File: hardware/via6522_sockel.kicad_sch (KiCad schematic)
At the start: 3 parts, among them IC2 VIA6522, P1 VIA_PIN_1-20, P2 VIA_PIN_21-40

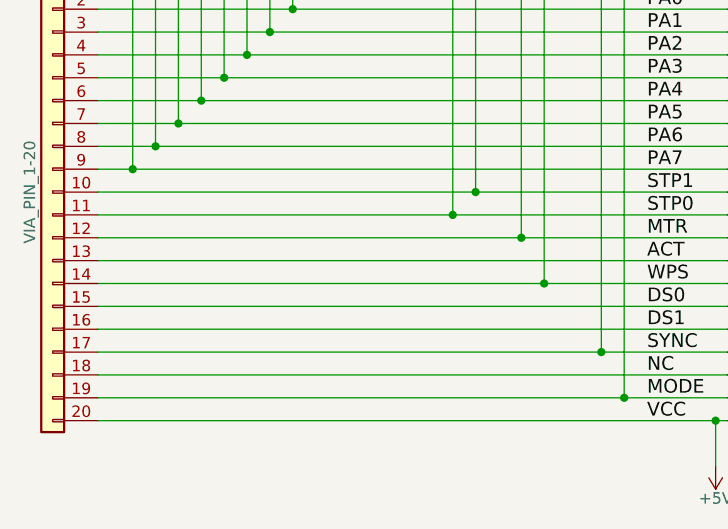
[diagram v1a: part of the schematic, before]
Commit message: fix WPS cross-driving
connection between 1541-board and VIA cut off
no cross driving of existing 74LS04 and Pico avoided
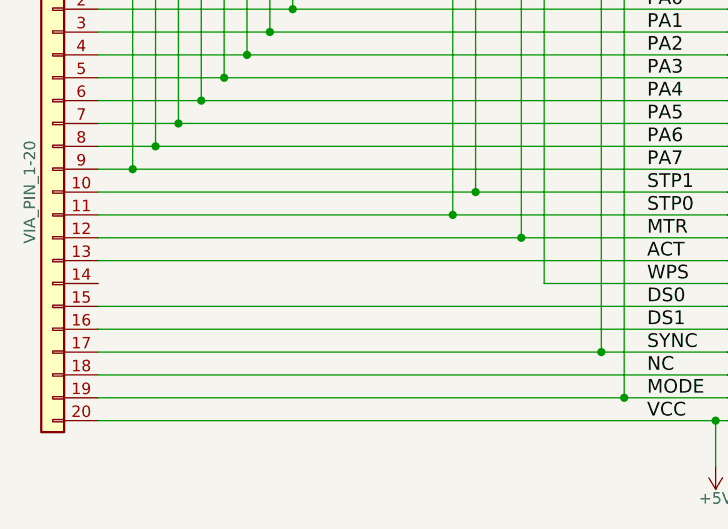
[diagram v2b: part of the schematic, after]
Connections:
- net WPS: no longer P1.14 (Pin_14)
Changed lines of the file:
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@@
-	)
-	(junction
-		(at 128.27 101.6)
-		(diameter 0)
-		(color 0 0 0 0)
 	)
 	(junction
@@
 		)
 		(stroke
-			(width 0)
-			(type default)
-		)
-	)
-	(wire
-		(pts
-			(xy 128.27 101.6) (xy 78.74 101.6)
-		)
-		(stroke
